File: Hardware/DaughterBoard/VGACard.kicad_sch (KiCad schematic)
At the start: 16 parts, among them J6 VGA_OUT, U2 ATmega1284P-PU, U4 ATmega328P-PU, U5 AS6C62256, U6 74HC365

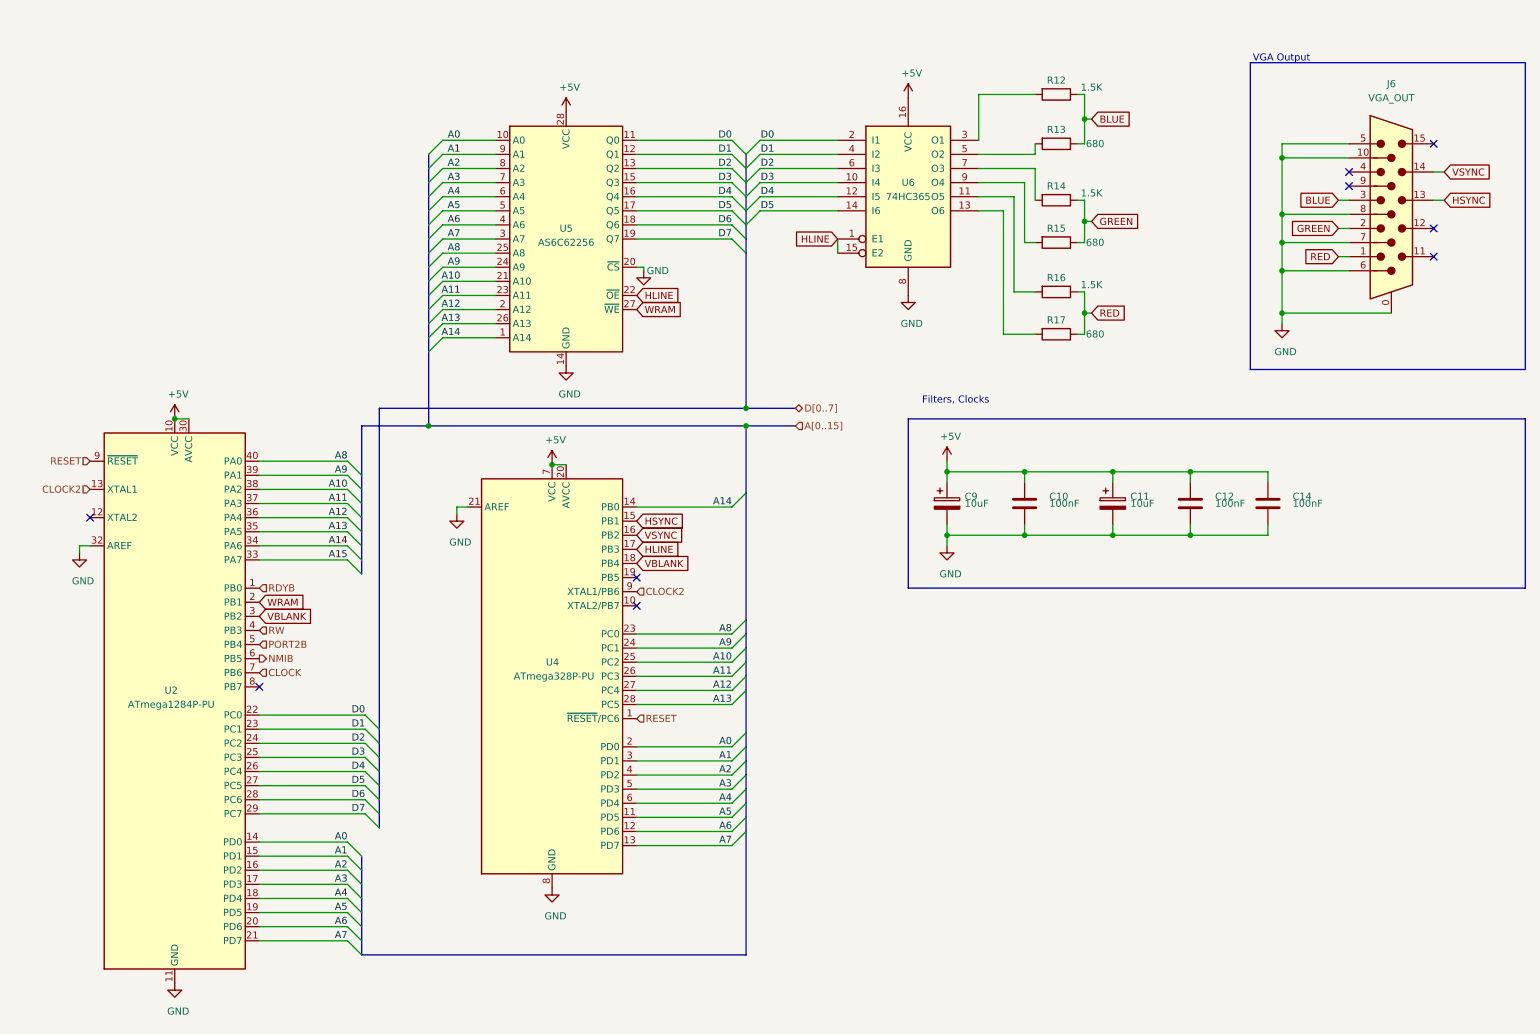
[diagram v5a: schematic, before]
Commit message: New PLD logic, VGA, DMA ...
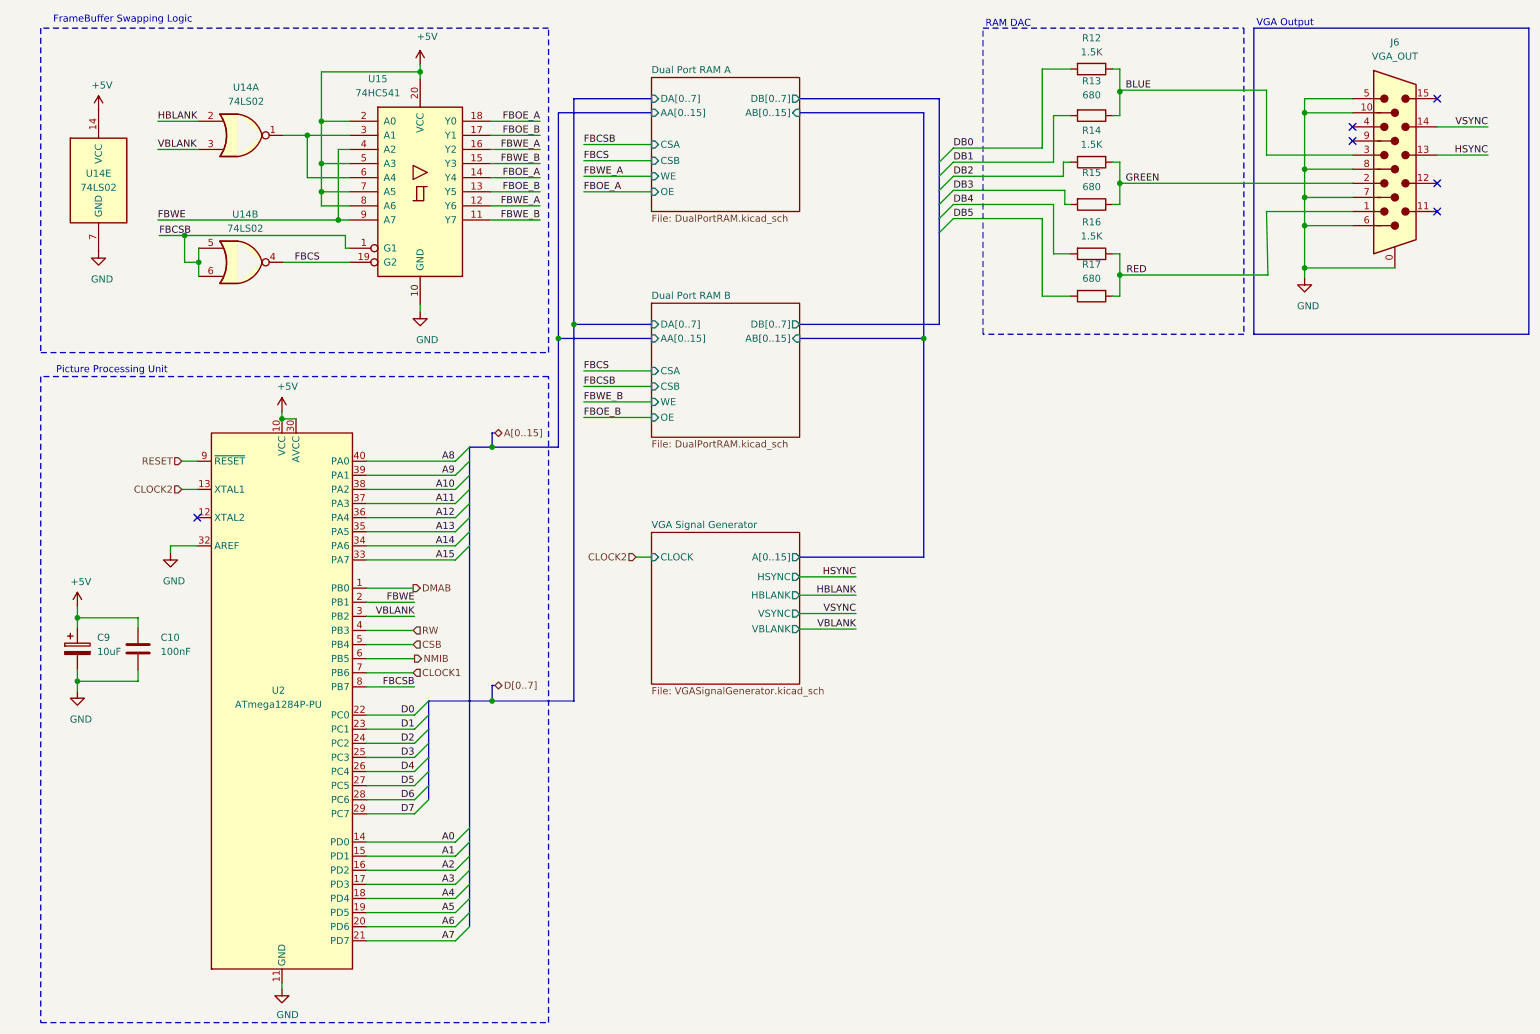
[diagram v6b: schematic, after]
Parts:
- removed C11: 10uF, Capacitor_THT:C_Radial_D5.0mm_H11.0mm_P2.00mm, symbol Device:CP
- removed C12, C14: 100nF, Capacitor_THT:C_Disc_D5.0mm_W2.5mm_P2.50mm, symbol Device:C
- removed U4: ATmega328P-PU, Package_DIP:DIP-28_W7.62mm, symbol MCU_Microchip_ATmega:ATmega328P-PU
- removed U5: AS6C62256, Package_DIP:DIP-28_W15.24mm, symbol Memory_RAM:HM62256BLP
- removed U6: 74HC365, Package_DIP:DIP-16_W7.62mm, symbol 74xx:74LS365
- added U14: 74LS02, symbol 74xx:74LS02
- added U15: 74HC541, Package_DIP:DIP-20_W7.62mm, symbol 74xx:74HCT541
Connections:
- net +5V: now also U14.14 (VCC), U15.2 (A0), U15.20 (VCC), U15.5 (A3), U15.7 (A5), U15.8 (A6)
- net GND: now also U14.7 (GND), U15.10 (GND)
- net VBLANK: now also U14.3
- net FBCSB: now reaches U2.8 (PB7)
- net FBCSB: now also U14.5, U14.6, U15.1 (G1)
- net DB2: now reaches R14.2
- net DB5: now reaches R17.2
- net DB0: now reaches R12.2
- net DB1: now reaches R13.2
- net DB3: now reaches R15.2
- net DB4: now reaches R16.2
- net CLOCK renamed CLOCK1
- net PORT2B renamed CSB
- net RDYB renamed DMAB
- net WRAM renamed FBWE
- net FBWE: now also U15.4 (A2), U15.9 (A7)
- new net: U14.1, U15.3 (A1), U15.6 (A4)
- new net FBCS: U14.4, U15.19 (G2)
- new net FBOE_A: U15.14 (Y4), U15.18 (Y0)
- new net FBOE_B: U15.13 (Y5), U15.17 (Y1)
- new net FBWE_A: U15.12 (Y6), U15.16 (Y2)
- new net FBWE_B: U15.11 (Y7), U15.15 (Y3)
- new net HBLANK: U14.2
- no-connect marks 9 -> 6
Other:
- added sheet Dual Port RAM A (DualPortRAM.kicad_sch)
- added sheet Dual Port RAM B (DualPortRAM.kicad_sch)
- added sheet VGA Signal Generator (VGASignalGenerator.kicad_sch)
- note added: "FrameBuffer Swapping Logic"
- note added: "Picture Processing Unit"
- note added: "RAM DAC"
- note removed: "Filters, Clocks"
- moved on the sheet: C10, C9, J6, R12, R13, R14, R15, R16, R17, U2

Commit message: Fix
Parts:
- U14: value 74LS02 -> 74HC00; symbol 74xx:74LS02 -> 74xx:74LS00
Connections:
- net FBCS: now also U14.5, U15.1 (G1), U2.8 (PB7); no longer U15.19 (G2)
- net FBCSB: now also U15.19 (G2); no longer U14.5, U15.1 (G1), U2.8 (PB7)
- net HBLANK: now also U14.1; no longer U14.2
- net VBLANK: now also U14.2; no longer U14.3
- net at U15.3 (A1), U15.6 (A4): now also U14.3; no longer U14.1
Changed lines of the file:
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@@
   (junction (at 174.244 73.152) (diameter 1.016) (color 0 0 0 0))
   (no_connect (at 251.46 35.052))
+  (no_connect (at 251.46 37.592))
+  (no_connect (at 43.434 105.41))
+  (no_connect (at 266.7 50.292))
+  (no_connect (at 266.7 45.212))
   (no_connect (at 266.7 29.972))
-  (no_connect (at 43.434 105.41))
-  (no_connect (at 266.7 45.212))
-  (no_connect (at 251.46 37.592))
-  (no_connect (at 266.7 50.292))
   (bus_entry (at 82.55 140.97) (size 2.54 -2.54)
     (stroke (width 0.1524) (type solid) (color 0 0 0 0))
@@
     (effects (font (size 1.27 1.27)) (justify left bottom))
   )
-  (label "FBCSB" (at 36.576 54.61 0)
-    (effects (font (size 1.27 1.27)) (justify left bottom))
-  )
-  (label "FBCS" (at 60.96 59.436 0)
+  (label "FBCS" (at 36.576 54.61 0)
+    (effects (font (size 1.27 1.27)) (justify left bottom))
+  )
+  (label "FBCSB" (at 60.96 59.436 0)
     (effects (font (size 1.27 1.27)) (justify left bottom))
   )
@@
     (effects (font (size 1.27 1.27)) (justify right bottom))
   )
-  (label "FBCSB" (at 82.55 135.89 180)
+  (label "FBCS" (at 82.55 135.89 180)
     (effects (font (size 1.27 1.27)) (justify right bottom))
   )
@@
     )
   )
-  (symbol (lib_id "74xx:74LS02") (at 51.308 36.576 0) (unit 1)
+  (symbol (lib_id "74xx:74LS00") (at 51.308 36.576 0) (unit 1)
     (in_bom yes) (on_board yes)
     (property "Reference" "U14" (id 0) (at 52.197 27.94 0))
-    (property "Value" "74LS02" (id 1) (at 52.197 30.48 0))
+    (property "Value" "74HC00" (id 1) (at 52.197 30.48 0))
     (property "Footprint" "" (id 2) (at 51.308 36.576 0)
       (effects (font (size 1.27 1.27)) hide)
@@
     )
   )
-  (symbol (lib_name "74xx:74LS02_2") (lib_id "74xx:74LS02") (at 51.308 59.436 0) (unit 2)
+  (symbol (lib_name "74xx:74LS02_2") (lib_id "74xx:74LS00") (at 51.308 59.436 0) (unit 2)
     (in_bom yes) (on_board yes)
     (property "Reference" "U14" (id 0) (at 52.07 50.8 0))
-    (property "Value" "74LS02" (id 1) (at 52.07 53.34 0))
+    (property "Value" "74HC00" (id 1) (at 52.07 53.34 0))
     (property "Footprint" "" (id 2) (at 51.308 59.436 0)
       (effects (font (size 1.27 1.27)) hide)
@@
     )
   )
-  (symbol (lib_name "74xx:74LS02_1") (lib_id "74xx:74LS02") (at 25.654 44.704 0) (unit 5)
+  (symbol (lib_name "74xx:74LS02_1") (lib_id "74xx:74LS00") (at 25.654 44.704 0) (unit 5)
     (in_bom yes) (on_board yes)
     (property "Reference" "U14" (id 0) (at 25.654 43.434 0))
-    (property "Value" "74LS02" (id 1) (at 25.654 45.974 0))
+    (property "Value" "74HC00" (id 1) (at 25.654 45.974 0))
     (property "Footprint" "" (id 2) (at 25.654 44.704 0)
       (effects (font (size 1.27 1.27)) hide)

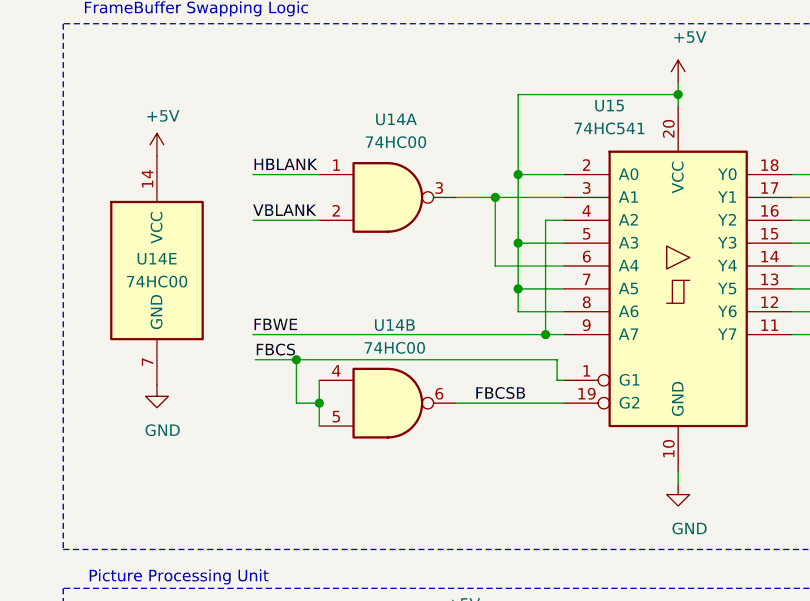
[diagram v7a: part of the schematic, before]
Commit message: Update to Kicad 6.0
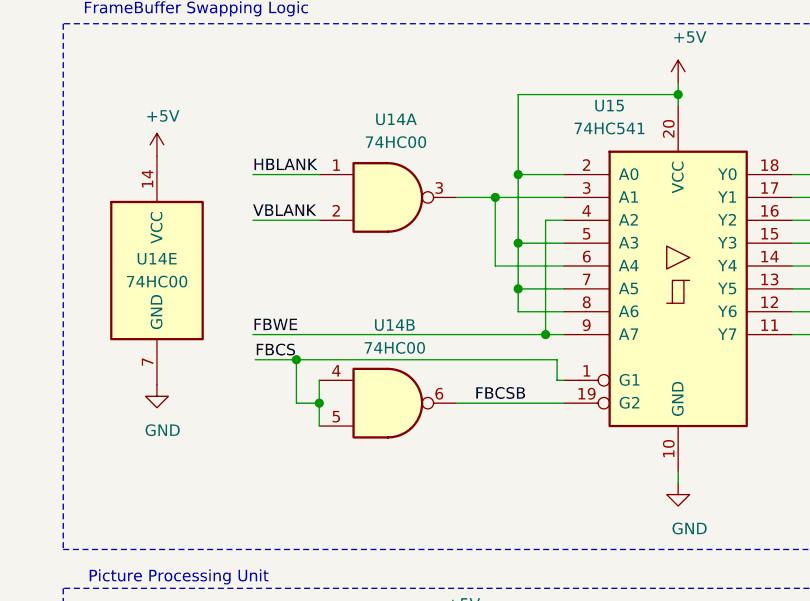
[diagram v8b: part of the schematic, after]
